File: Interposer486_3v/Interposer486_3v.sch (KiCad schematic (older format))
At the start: 170 parts, among them J1 WB/~WT, J2 CLKMUL

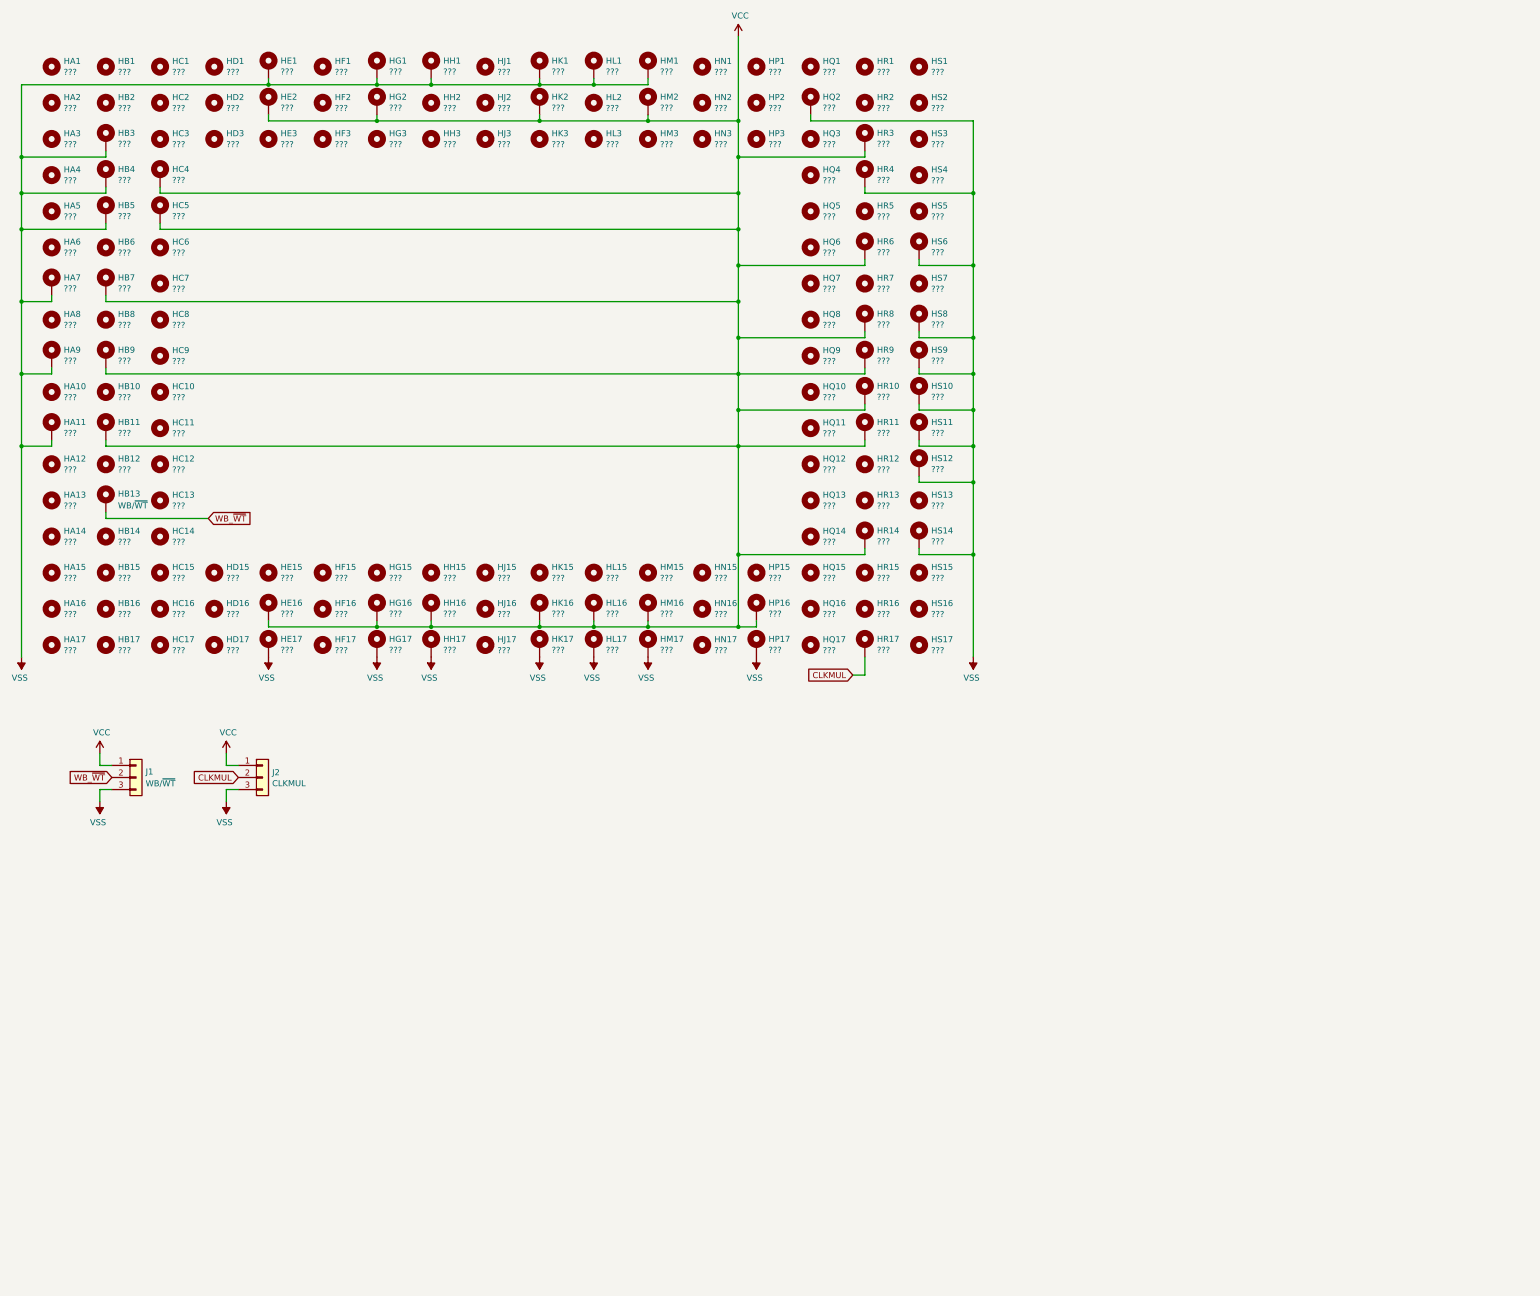
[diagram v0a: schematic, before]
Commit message: Completed first pass of layout of 486 3v interposer.
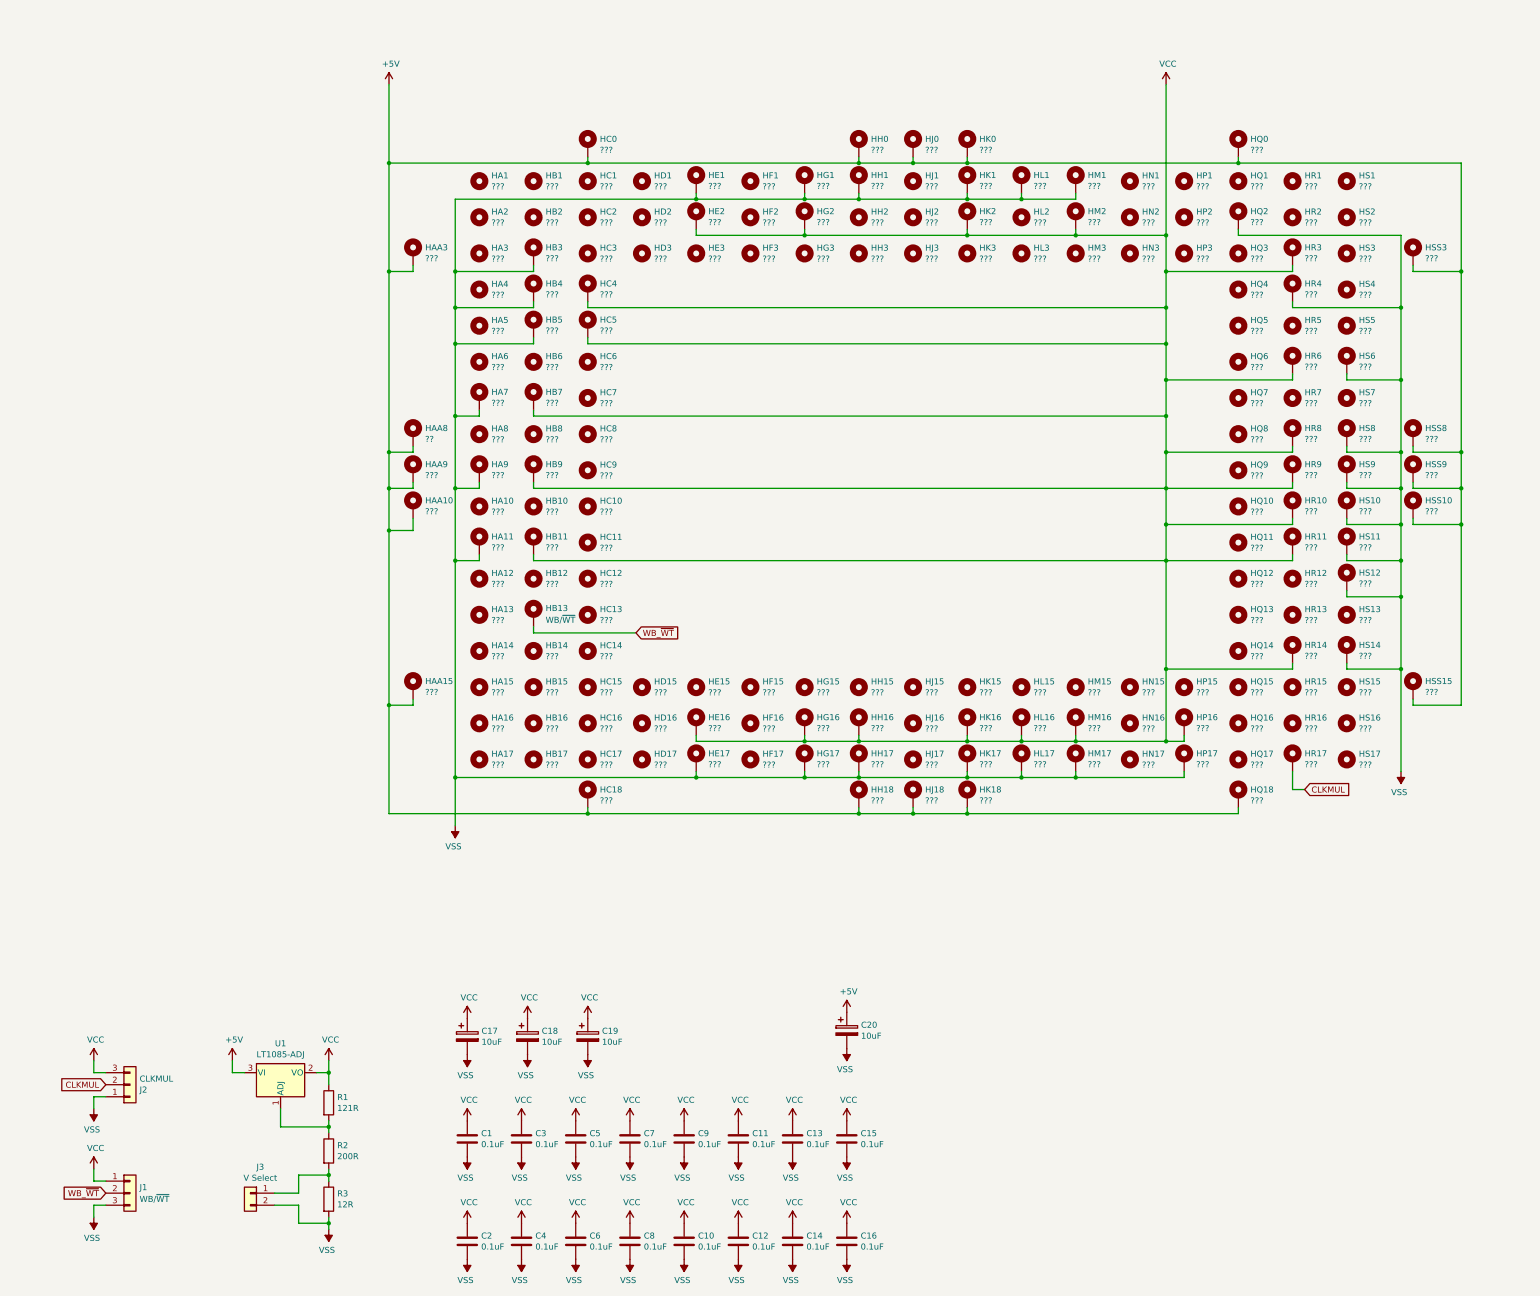
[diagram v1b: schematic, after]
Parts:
- added C1, C10, C11, C12, C13, C14, C15, C16, C2, C3, C4, C5, C6, C7, C8, C9: 0.1uF, Capacitor_SMD:C_1206_3216Metric, symbol Device:C
- added C17, C18, C19, C20: 10uF, Capacitor_Tantalum_SMD:CP_EIA-3216-10_Kemet-I, symbol Device:CP
- added HAA10, HAA15, HAA3, HAA9, HC0, HC18, HH0, HH18, HJ0, HJ18, HK0, HK18, HQ0, HQ18, HSS10, HSS15, HSS3, HSS8, HSS9: ???, 00Custom:MachinePinHole, symbol Mechanical:MountingHole_Pad
- added HAA8: ??, 00Custom:MachinePinHole, symbol Mechanical:MountingHole_Pad
- added J3: V Select, Connector_PinHeader_2.54mm:PinHeader_1x02_P2.54mm_Vertical_SMD_Pin1Left, symbol Connector_Generic:Conn_01x02
- added R1: 121R, Resistor_SMD:R_1206_3216Metric, symbol Device:R
- added R2: 200R, Resistor_SMD:R_1206_3216Metric, symbol Device:R
- added R3: 12R, Resistor_SMD:R_1206_3216Metric, symbol Device:R
- added U1: LT1085-ADJ, Package_TO_SOT_SMD:TO-263-3_TabPin2, symbol Regulator_Linear:LT1085-ADJ
- J1, J2: footprint Connector_PinHeader_2.54mm:PinHeader_1x03_P2.54mm_Vertical -> Connector_PinHeader_2.54mm:PinHeader_1x03_P2.54mm_Vertical_SMD_Pin1Left
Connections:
- net VCC: now also J2.3 (Pin_3), C1.1, C10.1, C11.1, C12.1, C13.1, C14.1, C15.1, C16.1, C17.1, C18.1, C19.1, C2.1, C3.1, C4.1, C5.1, C6.1, C7.1, C8.1, C9.1, R1.1, U1.2 (VO); no longer J2.1 (Pin_1)
- net VSS: now also J2.1 (Pin_1), C1.2, C10.2, C11.2, C12.2, C13.2, C14.2, C15.2, C16.2, C17.2, C18.2, C19.2, C2.2, C20.2, C3.2, C4.2, C5.2, C6.2, C7.2, C8.2, C9.2, J3.2 (Pin_2), R3.2; no longer J2.3 (Pin_3)
- new net: R1.2, R2.1, U1.1 (ADJ)
- new net: J3.1 (Pin_1), R2.2, R3.1
- new net +5V: C20.1, HAA10.1, HAA15.1, HAA3.1, HAA8.1, HAA9.1, HC0.1, HC18.1, HH0.1, HH18.1, HJ0.1, HJ18.1, HK0.1, HK18.1, HQ0.1, HQ18.1, HSS10.1, HSS15.1, HSS3.1, HSS8.1, HSS9.1, U1.3 (VI)
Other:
- moved on the sheet: HA1, HA10, HA11, HA12, HA13, HA14, HA15, HA16, HA17, HA2, HA3, HA4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

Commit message: Jig hole wip
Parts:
- added HDT1, HDT10, HDT11, HDT12, HDT13, HDT14, HDT15, HDT16, HDT17, HDT18, HDT19, HDT2, HDT20, HDT21, HDT22, HDT23, HDT24, HDT25, HDT26, HDT27, HDT28, HDT3, HDT4, HDT5, HDT6, HDT7, HDT8, HDT9: ???, 00Custom:MachinePinHole, symbol Mechanical:MountingHole
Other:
- moved on the sheet: HA1, HA10, HA11, HA12, HA13, HA14, HA15, HA16, HA17, HA2, HA3, HA4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

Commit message: Finished first pass of 486 3v interposer.
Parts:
- removed HDT10, HDT11, HDT12, HDT13, HDT14, HDT15, HDT16, HDT17, HDT18, HDT19, HDT2, HDT20, HDT21, HDT22, HDT23, HDT24, HDT25, HDT26, HDT27, HDT28, HDT3, HDT4, HDT5, HDT6, HDT7, HDT8, HDT9: ???, 00Custom:MachinePinHole, symbol Mechanical:MountingHole
- added HDT10, HDT11, HDT12, HDT13, HDT14, HDT15, HDT16, HDT17, HDT18, HDT19, HDT2, HDT20, HDT21, HDT22, HDT23, HDT24, HDT25, HDT26, HDT27, HDT28, HDT3, HDT4, HDT5, HDT6, HDT7, HDT8, HDT9: ???, 00Custom:MachinePinHole, symbol Mechanical:MountingHole_Pad
- HDT1: symbol Mechanical:MountingHole -> Mechanical:MountingHole_Pad
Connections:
- net VSS: now also HDT1.1, HDT10.1, HDT11.1, HDT12.1, HDT13.1, HDT14.1, HDT15.1, HDT16.1, HDT17.1, HDT18.1, HDT19.1, HDT2.1, HDT20.1, HDT21.1, HDT22.1, HDT23.1, HDT24.1, HDT25.1, HDT26.1, HDT27.1, HDT28.1, HDT3.1, HDT4.1, HDT5.1, HDT6.1, HDT7.1, HDT8.1, HDT9.1
